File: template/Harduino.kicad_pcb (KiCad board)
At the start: 2 copper layers, 40.6 x 40.6 mm, 24 parts, among them J1 2, J10 11, J11 12, J12 13, J13 A0, J14 A1, J15 A2, J16 A3, J17 A4, J18 A5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

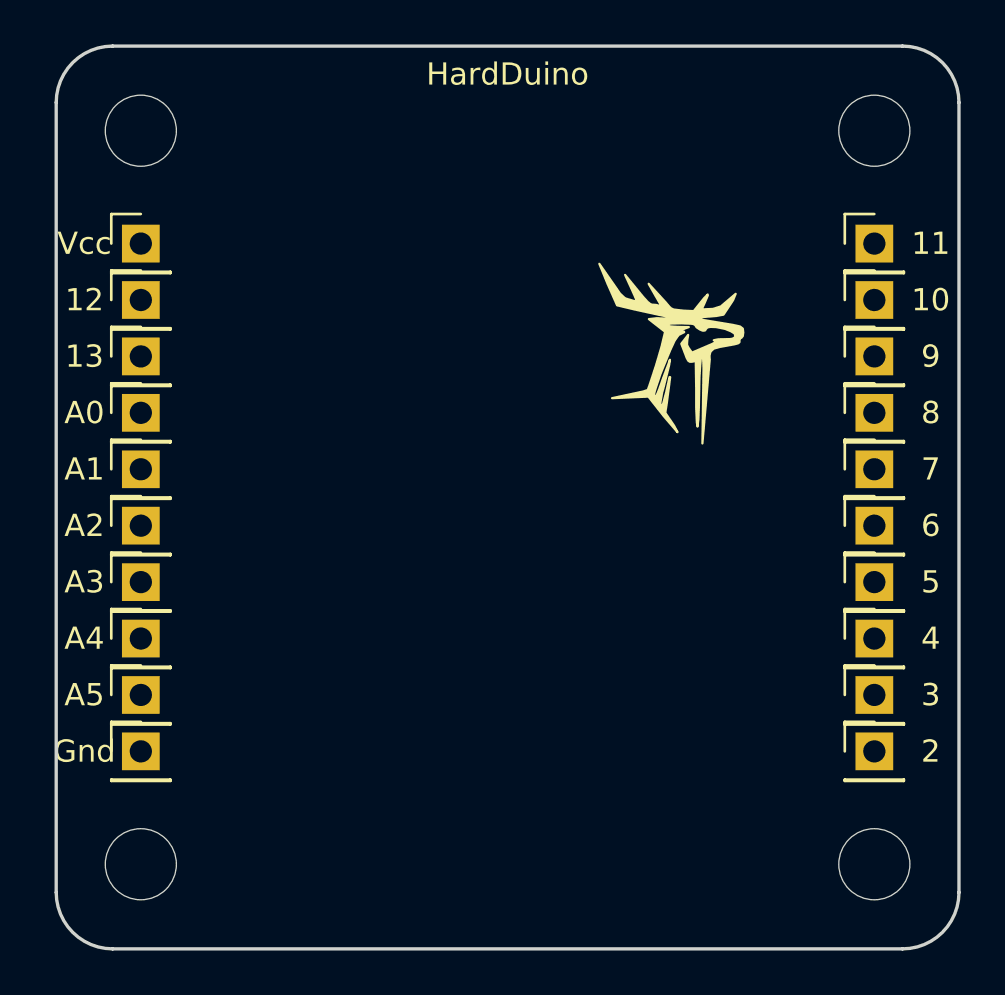
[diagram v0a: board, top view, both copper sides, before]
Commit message: Replace 10 x 1pin sockets -> 1 x 10pin socket
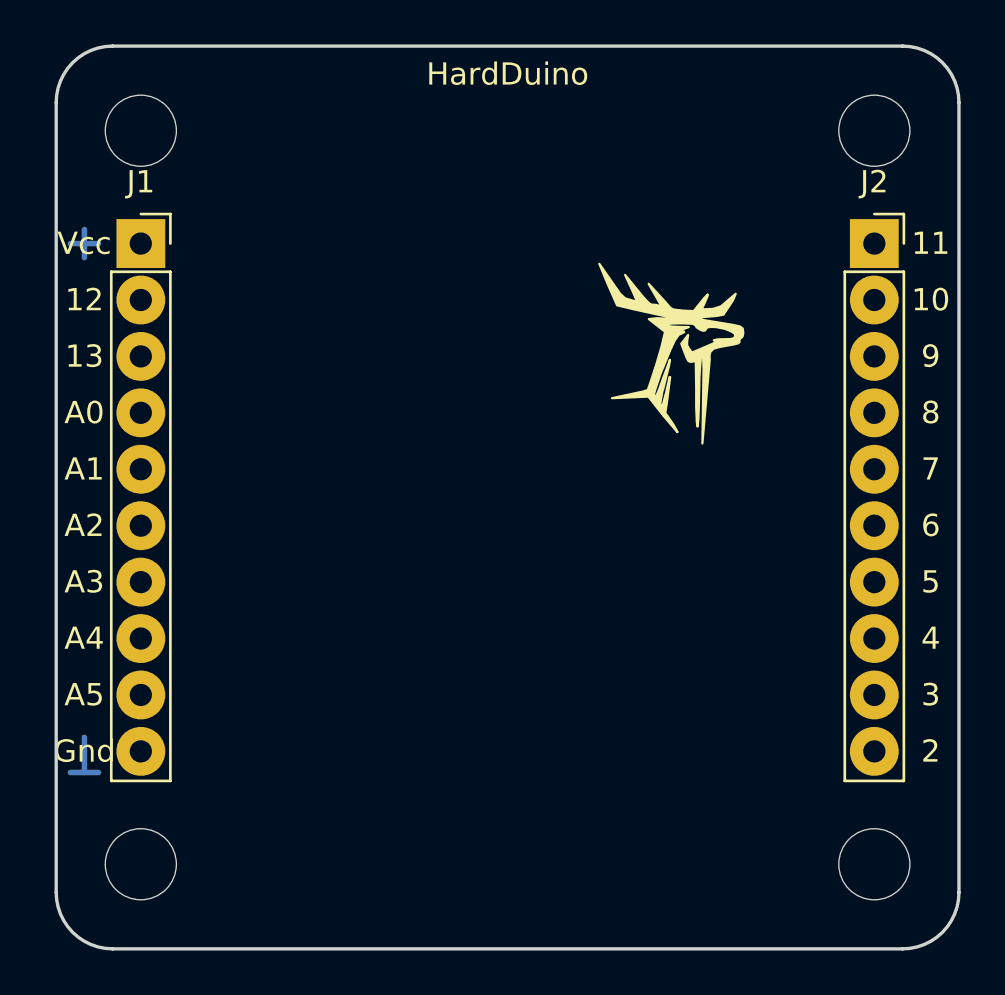
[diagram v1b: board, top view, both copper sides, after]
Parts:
- removed J10: 11, Connector_PinHeader_2.54mm:PinHeader_1x01_P2.54mm_Vertical
- removed J11: 12, Connector_PinHeader_2.54mm:PinHeader_1x01_P2.54mm_Vertical
- removed J12: 13, Connector_PinHeader_2.54mm:PinHeader_1x01_P2.54mm_Vertical
- removed J13: A0, Connector_PinHeader_2.54mm:PinHeader_1x01_P2.54mm_Vertical
- removed J14: A1, Connector_PinHeader_2.54mm:PinHeader_1x01_P2.54mm_Vertical
- removed J15: A2, Connector_PinHeader_2.54mm:PinHeader_1x01_P2.54mm_Vertical
- removed J16: A3, Connector_PinHeader_2.54mm:PinHeader_1x01_P2.54mm_Vertical
- removed J17: A4, Connector_PinHeader_2.54mm:PinHeader_1x01_P2.54mm_Vertical
- removed J18: A5, Connector_PinHeader_2.54mm:PinHeader_1x01_P2.54mm_Vertical
- removed J19: Vcc, Connector_PinHeader_2.54mm:PinHeader_1x01_P2.54mm_Vertical
- removed J20: Gnd, Connector_PinHeader_2.54mm:PinHeader_1x01_P2.54mm_Vertical
- removed J3: 4, Connector_PinHeader_2.54mm:PinHeader_1x01_P2.54mm_Vertical
- removed J4: 5, Connector_PinHeader_2.54mm:PinHeader_1x01_P2.54mm_Vertical
- removed J5: 6, Connector_PinHeader_2.54mm:PinHeader_1x01_P2.54mm_Vertical
- removed J6: 7, Connector_PinHeader_2.54mm:PinHeader_1x01_P2.54mm_Vertical
- removed J7: 8, Connector_PinHeader_2.54mm:PinHeader_1x01_P2.54mm_Vertical
- removed J8: 9, Connector_PinHeader_2.54mm:PinHeader_1x01_P2.54mm_Vertical
- removed J9: 10, Connector_PinHeader_2.54mm:PinHeader_1x01_P2.54mm_Vertical
- J1: value 2 -> Conn_01x10_Male; footprint Connector_PinHeader_2.54mm:PinHeader_1x01_P2.54mm_Vertical -> Connector_PinSocket_2.54mm:PinSocket_1x10_P2.54mm_Vertical
- J2: value 3 -> Conn_01x10_Male; footprint Connector_PinHeader_2.54mm:PinHeader_1x01_P2.54mm_Vertical -> Connector_PinSocket_2.54mm:PinSocket_1x10_P2.54mm_Vertical
- moved J1 40.2 mm to (92.7, 59.7)
- moved J2 20.3 mm to (125.7, 59.7)
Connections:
- net Net-(J1-Pad1) renamed VCC
- net Net-(J2-Pad1) renamed /11
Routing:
- net (no net): track 0.00 -> 5.40 mm

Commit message: Add version, date and git hash Fix pinheader pad sizes
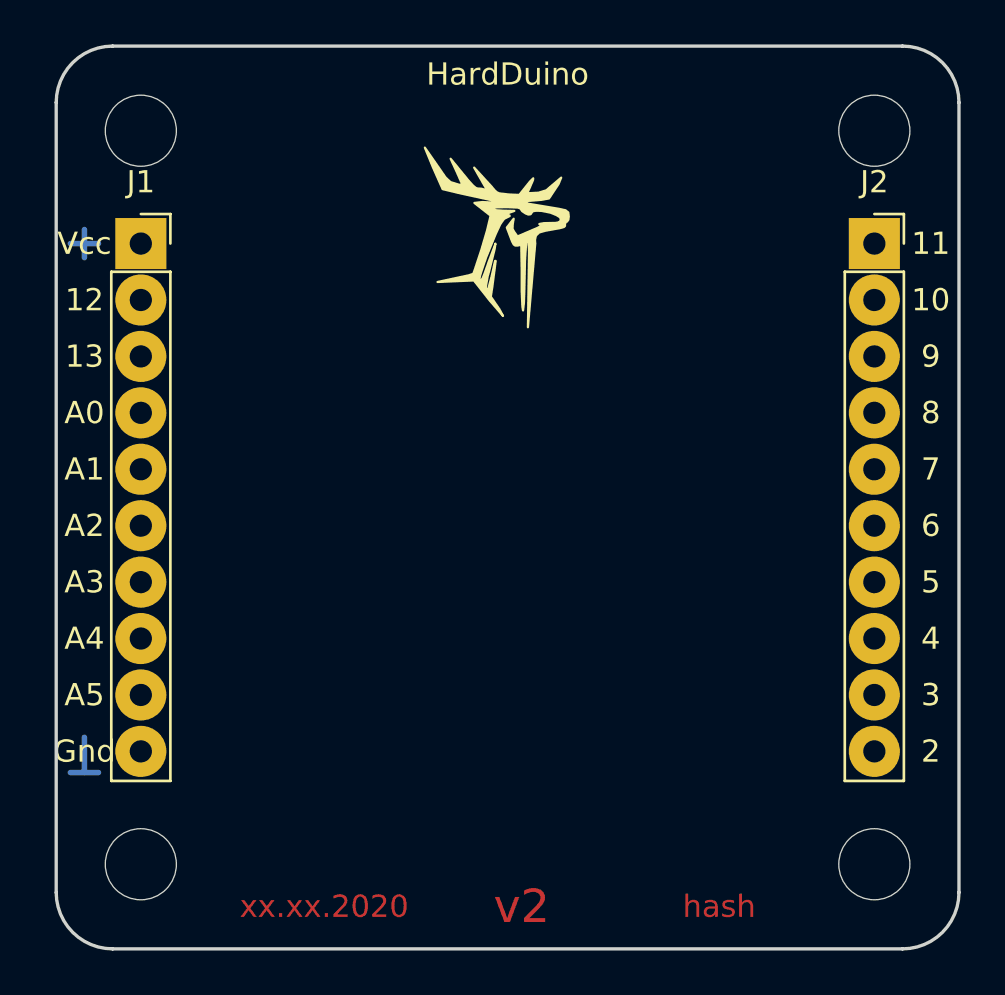
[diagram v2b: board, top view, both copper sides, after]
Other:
- board text added: "hash"
- board text added: "v2"
- board text added: "xx.xx.2020"
